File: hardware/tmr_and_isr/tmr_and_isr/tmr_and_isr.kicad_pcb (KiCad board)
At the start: 2 copper layers, 80 x 30 mm, 23 parts, among them J0 Conn_01x10, J1 Conn_01x10, J2 Conn_01x10, J3 Conn_01x12_Male, U1 74LS04, U2 4072, U3 74LS10, U4 74HC00, U6 74HC00, U7 74LS10

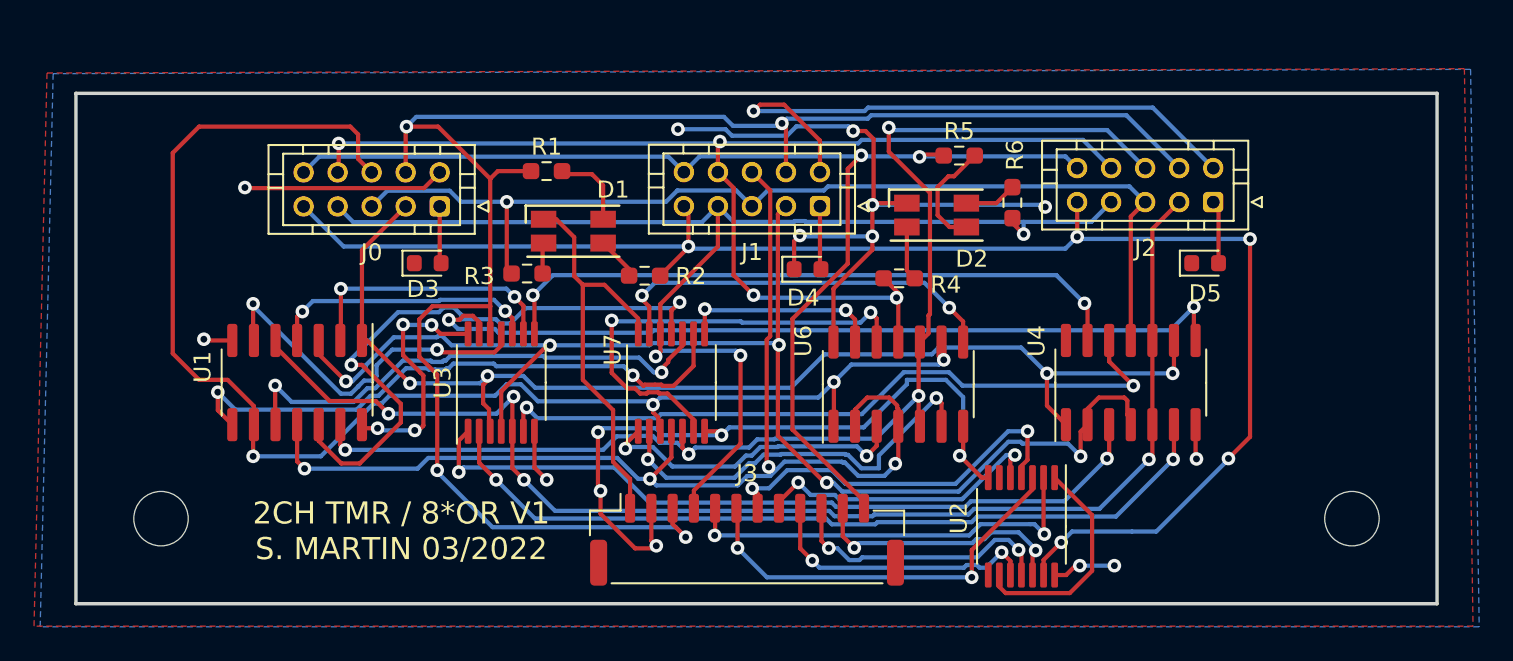
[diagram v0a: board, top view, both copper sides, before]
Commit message: Added updated TMR and ISR PCB
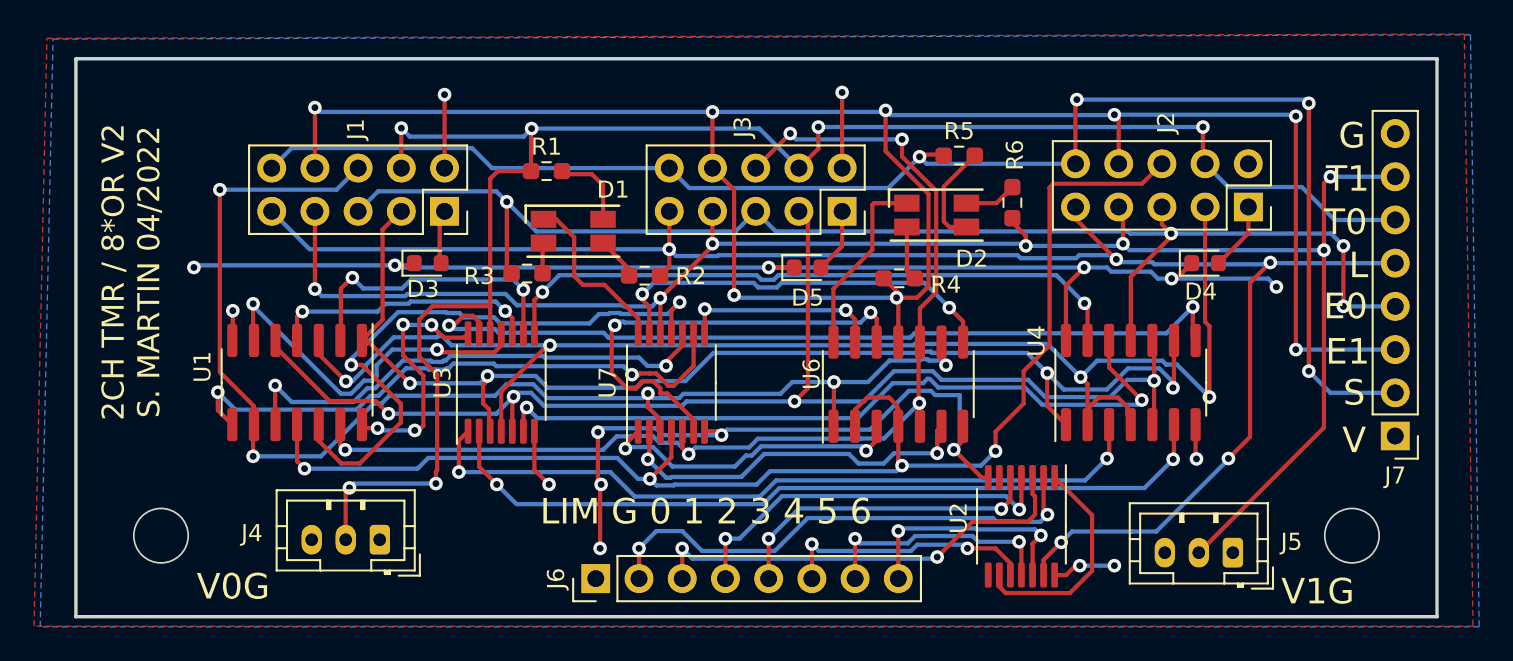
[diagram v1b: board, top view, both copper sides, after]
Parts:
- removed J0: Conn_01x10, Connector_JST:JST_PHD_B10B-PHDSS_2x05_P2.00mm_Vertical
- removed REF** (x2): MountingHole_3.2mm_M3, MountingHole:MountingHole_3.2mm_M3
- added J4: Conn_01x03, Connector_JST:JST_PH_B3B-PH-K_1x03_P2.00mm_Vertical, F.Cu at (117.9, 126.2)
- added J5: Conn_01x03, Connector_JST:JST_PH_B3B-PH-K_1x03_P2.00mm_Vertical, F.Cu at (168.0, 127.0)
- added J6: Conn_01x08, Connector_PinHeader_2.54mm:PinHeader_1x08_P2.54mm_Vertical, F.Cu at (130.6, 128.5)
- added J7: Conn_01x08, Connector_PinHeader_2.54mm:PinHeader_1x08_P2.54mm_Vertical, F.Cu at (177.5, 120.1)
- J1, J2: value Conn_01x10 -> Conn_02x05_Odd_Even; footprint Connector_JST:JST_PHD_B10B-PHDSS_2x05_P2.00mm_Vertical -> Connector_PinSocket_2.54mm:PinSocket_2x05_P2.54mm_Vertical
- J3: value Conn_01x12_Male -> Conn_02x05_Odd_Even; footprint Connector_JST:JST_GH_SM12B-GHS-TB_1x12-1MP_P1.25mm_Horizontal -> Connector_PinSocket_2.54mm:PinSocket_2x05_P2.54mm_Vertical
- moved D4 23.4 mm to (166.4, 110.0)
- moved D5 23.4 mm to (143.0, 110.2)
- moved J1 22.1 mm to (121.7, 106.9), turned to -90 degrees
- moved J3 20.1 mm to (145.0, 106.9), turned to -90 degrees
- moved J2 2.08 mm to (168.9, 106.7), turned to -90 degrees
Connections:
- J1 pad 1: /VCC1 -> /VCC0
- J1 pad 3: /TM0_1 -> /TM0_0
- J1 pad 6: /TM1_1 -> /TM1_0
- J2 pad 1: /VCC2 -> /VCC1
- J2 pad 3: /TM0_2 -> /TM0_1
- J2 pad 6: /TM1_2 -> /TM1_1
- J3 pad 1: VCC -> /VCC2
- J3 pad 10: /LIM5 -> /SYNC
- J3 pad 3: /TM0_OUT -> /TM0_2
- J3 pad 4: /TM1_OUT -> /TM0_OUT
- J3 pad 5: /LIM0 -> /TM0_ERR
- J3 pad 6: /LIM1 -> /TM1_2
- J3 pad 7: /LIM2 -> /TM1_OUT
- J3 pad 8: /LIM3 -> /TM1_ERR
- J3 pad 9: /LIM4 -> /LIM_OUT
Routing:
- net /TM1_ERR: track 70.5 -> 122.6 mm, vias 4 -> 8
- net GND: track 97.8 -> 54.4 mm
- net /TM1_OUT: track 74.8 -> 103.6 mm, vias 3 -> 7
- net VCC: track 86.4 -> 112.8 mm
- net /TM0_ERR: track 60.5 -> 80.7 mm, vias 1 -> 4
- net /SYNC: track 72.6 -> 90.1 mm, vias 2 -> 4
- net /TM1_1: track 68.4 -> 80.0 mm
- net /LIM_OUT: track 91.6 -> 102.7 mm
- net /TM1_0: track 84.5 -> 75.9 mm, vias 4 -> 5
- net /TM1_2: track 74.3 -> 66.6 mm, vias 4 -> 5
- net /LIM0: track 24.8 -> 30.0 mm
- net /TM0_1: track 77.9 -> 82.8 mm, vias 5 -> 4
- net /TM0_0: track 68.7 -> 70.9 mm
- net Net-(U6-Pad6): track 24.0 -> 21.9 mm
- net /LIM1: track 24.2 -> 26.1 mm
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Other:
- board size 80 x 30 mm -> 80 x 32.8 mm
- board text added: "2CH TMR / 8*OR V2 S. MARTIN 04/2022"
- board text added: "E0"
- board text added: "E1"
- board text added: "G"
- board text added: "L"
- board text added: "LIM G 0 1 2 3 4 5 6"
- board text added: "S"
- board text added: "T0"
- board text added: "T1"
- board text added: "V"
- board text added: "V0G"
- board text added: "V1G"
- board text removed: "2CH TMR / 8*OR V1 S. MARTIN 03/2022"

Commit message: Update tmr/isr circuit with TODOs, add tribot webots env vars and auto-switching between webots worlds
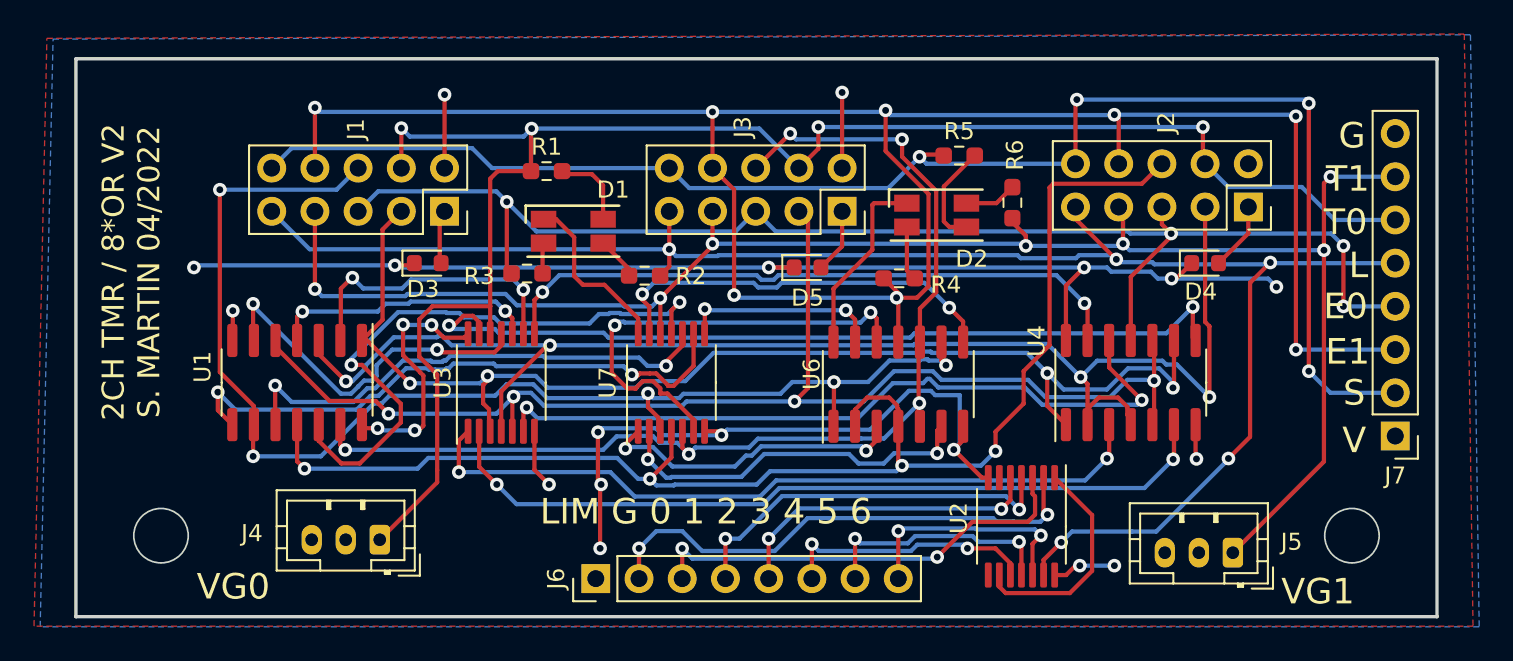
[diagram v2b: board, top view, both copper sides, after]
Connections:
- J4 pad 1: GND -> /TM0_OUT
- J4 pad 2: /TM0_OUT -> GND
- J5 pad 1: GND -> /TM1_OUT
- J5 pad 2: /TM1_OUT -> GND
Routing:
- net /TM0_OUT: track 104.5 -> 100.8 mm, vias 6 -> 4
- net /TM1_OUT: track 103.6 -> 102.8 mm
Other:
- board text added: "VG0"
- board text added: "VG1"
- board text removed: "V0G"
- board text removed: "V1G"
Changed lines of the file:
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@@
     (fp_line (start 5.95 -1.7) (end -1.95 -1.7) (layer "F.Fab") (width 0.1))
     (pad "1" thru_hole roundrect (at 0 0 180) (size 1.2 1.75) (drill 0.75) (layers *.Cu *.Mask) (roundrect_rratio 0.2083333333)
-      (net 2 "GND") (pinfunction "Pin_1") (pintype "passive"))
+      (net 25 "/TM0_OUT") (pinfunction "Pin_1") (pintype "passive"))
     (pad "2" thru_hole oval (at 2 0 180) (size 1.2 1.75) (drill 0.75) (layers *.Cu *.Mask)
-      (net 25 "/TM0_OUT") (pinfunction "Pin_2") (pintype "passive"))
+      (net 2 "GND") (pinfunction "Pin_2") (pintype "passive"))
     (pad "3" thru_hole oval (at 4 0 180) (size 1.2 1.75) (drill 0.75) (layers *.Cu *.Mask)
       (net 26 "VCC") (pinfunction "Pin_3") (pintype "passive"))
@@
     (fp_line (start -1.95 2.8) (end 5.95 2.8) (layer "F.Fab") (width 0.1))
     (pad "1" thru_hole roundrect (at 0 0 180) (size 1.2 1.75) (drill 0.75) (layers *.Cu *.Mask) (roundrect_rratio 0.2083333333)
-      (net 2 "GND") (pinfunction "Pin_1") (pintype "passive"))
+      (net 39 "/TM1_OUT") (pinfunction "Pin_1") (pintype "passive"))
     (pad "2" thru_hole oval (at 2 0 180) (size 1.2 1.75) (drill 0.75) (layers *.Cu *.Mask)
-      (net 39 "/TM1_OUT") (pinfunction "Pin_2") (pintype "passive"))
+      (net 2 "GND") (pinfunction "Pin_2") (pintype "passive"))
     (pad "3" thru_hole oval (at 4 0 180) (size 1.2 1.75) (drill 0.75) (layers *.Cu *.Mask)
       (net 26 "VCC") (pinfunction "Pin_3") (pintype "passive"))
@@
     (effects (font (size 1.5 1.5) (thickness 0.3)))
   )
-  (gr_text "V0G\n" (at 109.25 129) (layer "F.SilkS")
+  (gr_text "VG0" (at 109.25 129) (layer "F.SilkS")
     (effects (font (size 1.5 1.5) (thickness 0.3)))
   )
@@
     (effects (font (size 1.5 1.5) (thickness 0.3)))
   )
-  (gr_text "V1G" (at 173 129.286) (layer "F.SilkS")
+  (gr_text "VG1" (at 173 129.286) (layer "F.SilkS")
     (effects (font (size 1.5 1.5) (thickness 0.3)))
   )
@@
   (segment (start 142.494 104.394) (end 143.637 103.251) (width 0.25) (layer "F.Cu") (net 25))
   (segment (start 120.9546 112.5136) (end 120.179499 113.288701) (width 0.25) (layer "F.Cu") (net 25))
+  (segment (start 117.856 126.238) (end 121.2342 122.8598) (width 0.25) (layer "F.Cu") (net 25))
   (segment (start 120.179499 113.288701) (end 120.179499 115.480499) (width 0.25) (layer "F.Cu") (net 25))
   (segment (start 126.7479 104.5718) (end 124.7988 104.5718) (width 0.25) (layer "F.Cu") (net 25))
   (segment (start 166.243 101.981) (end 166.243 104.013) (width 0.25) (layer "F.Cu") (net 25))
   (segment (start 124.35 105.0206) (end 124.35 112.5136) (width 0.25) (layer "F.Cu") (net 25))
-  (segment (start 116.078 123.19) (end 115.856 123.412) (width 0.25) (layer "F.Cu") (net 25))
-  (segment (start 121.2342 122.154211) (end 121.158 122.230411) (width 0.25) (layer "F.Cu") (net 25))
   (segment (start 126.7479 104.5718) (end 126.7479 102.1061) (width 0.25) (layer "F.Cu") (net 25))
   (segment (start 124.7988 104.5718) (end 124.35 105.0206) (width 0.25) (layer "F.Cu") (net 25))
@@
   (segment (start 166.243 104.013) (end 166.37 104.14) (width 0.25) (layer "F.Cu") (net 25))
   (segment (start 124.35 112.5136) (end 124.35 114.1375) (width 0.25) (layer "F.Cu") (net 25))
+  (segment (start 121.2342 122.8598) (end 121.2342 122.154211) (width 0.25) (layer "F.Cu") (net 25))
   (segment (start 126.7479 102.1061) (end 126.783499 102.070501) (width 0.25) (layer "F.Cu") (net 25))
-  (segment (start 121.158 122.230411) (end 121.158 122.936) (width 0.25) (layer "F.Cu") (net 25))
-  (segment (start 115.856 123.412) (end 115.856 126.238) (width 0.25) (layer "F.Cu") (net 25))
   (segment (start 121.2342 116.5352) (end 121.2342 122.154211) (width 0.25) (layer "F.Cu") (net 25))
   (segment (start 120.179499 115.480499) (end 121.2342 116.5352) (width 0.25) (layer "F.Cu") (net 25))
   (segment (start 124.35 112.5136) (end 120.9546 112.5136) (width 0.25) (layer "F.Cu") (net 25))
   (via (at 143.637 101.981) (size 0.8) (drill 0.4) (layers "F.Cu" "B.Cu") (net 25))
-  (via (at 121.158 122.936) (size 0.8) (drill 0.4) (layers "F.Cu" "B.Cu") (net 25))
   (via (at 126.783499 102.070501) (size 0.8) (drill 0.4) (layers "F.Cu" "B.Cu") (net 25))
   (via (at 166.243 101.981) (size 0.8) (drill 0.4) (layers "F.Cu" "B.Cu") (net 25))
   (via (at 119.126 102.045478) (size 0.8) (drill 0.4) (layers "F.Cu" "B.Cu") (net 25))
-  (via (at 116.078 123.19) (size 0.8) (drill 0.4) (layers "F.Cu" "B.Cu") (net 25))
   (segment (start 172.053489 105.505489) (end 173.99 107.442) (width 0.25) (layer "B.Cu") (net 25))
   (segment (start 143.637 101.981) (end 166.243 101.981) (width 0.25) (layer "B.Cu") (net 25))
   (segment (start 140.170501 102.070501) (end 142.494 104.394) (width 0.25) (layer "B.Cu") (net 25))
   (segment (start 119.126 102.045478) (end 119.621523 102.541001) (width 0.25) (layer "B.Cu") (net 25))
-  (segment (start 121.158 122.936) (end 116.332 122.936) (width 0.25) (layer "B.Cu") (net 25))
-  (segment (start 116.332 122.936) (end 116.078 123.19) (width 0.25) (layer "B.Cu") (net 25))
   (segment (start 166.37 104.14) (end 167.735489 105.505489) (width 0.25) (layer "B.Cu") (net 25))
   (segment (start 167.735489 105.505489) (end 172.053489 105.505489) (width 0.25) (layer "B.Cu") (net 25))
@@
   (segment (start 137.037009 112.7506) (end 145.2505 112.7506) (width 0.25) (layer "B.Cu") (net 38))
   (segment (start 173.355 105.283) (end 173.736 104.902) (width 0.25) (layer "F.Cu") (net 39))
+  (segment (start 168 127) (end 173.355 121.645) (width 0.25) (layer "F.Cu") (net 39))
   (segment (start 173.355 109.22) (end 173.355 105.283) (width 0.25) (layer "F.Cu") (net 39))
   (segment (start 155.829 108.966) (end 155.829 108.3685) (width 0.25) (layer "F.Cu") (net 39))
+  (segment (start 173.355 121.645) (end 173.355 109.22) (width 0.25) (layer "F.Cu") (net 39))
   (segment (start 134.35 112.03) (end 134.35 114.1375) (width 0.25) (layer "F.Cu") (net 39))
   (segment (start 137.414 106.934) (end 137.414 108.839) (width 0.25) (layer "F.Cu") (net 39))
   (segment (start 114.046 106.934) (end 114.046 111.506) (width 0.25) (layer "F.Cu") (net 39))
-  (segment (start 166 127) (end 173.355 119.645) (width 0.25) (layer "F.Cu") (net 39))
   (segment (start 155.829 108.3685) (end 155.0416 107.5811) (width 0.25) (layer "F.Cu") (net 39))
   (segment (start 137.414 108.839) (end 137.414 108.966) (width 0.25) (layer "F.Cu") (net 39))
   (segment (start 161.544 108.839) (end 161.544 106.934) (width 0.25) (layer "F.Cu") (net 39))
   (segment (start 155.0416 107.5811) (end 155.0416 107.3404) (width 0.25) (layer "F.Cu") (net 39))
-  (segment (start 173.355 109.22) (end 173.355 119.645) (width 0.25) (layer "F.Cu") (net 39))
   (segment (start 161.544 106.934) (end 161.29 106.68) (width 0.25) (layer "F.Cu") (net 39))
   (segment (start 137.414 108.966) (end 134.35 112.03) (width 0.25) (layer "F.Cu") (net 39))
